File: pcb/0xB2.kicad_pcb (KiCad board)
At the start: 2 copper layers, 17.8 x 33 mm, 37 parts, among them J1 USB_C_Receptacle_USB2.0, J2 Conn_01x12, J3 Conn_01x05, J4 Conn_01x12, SW1 SW_Push, SW2 SW_Push, U1 RP2040, U2 W25Q32JVZP, U3 AP2127K-3.3, Y1 Crystal_GND24

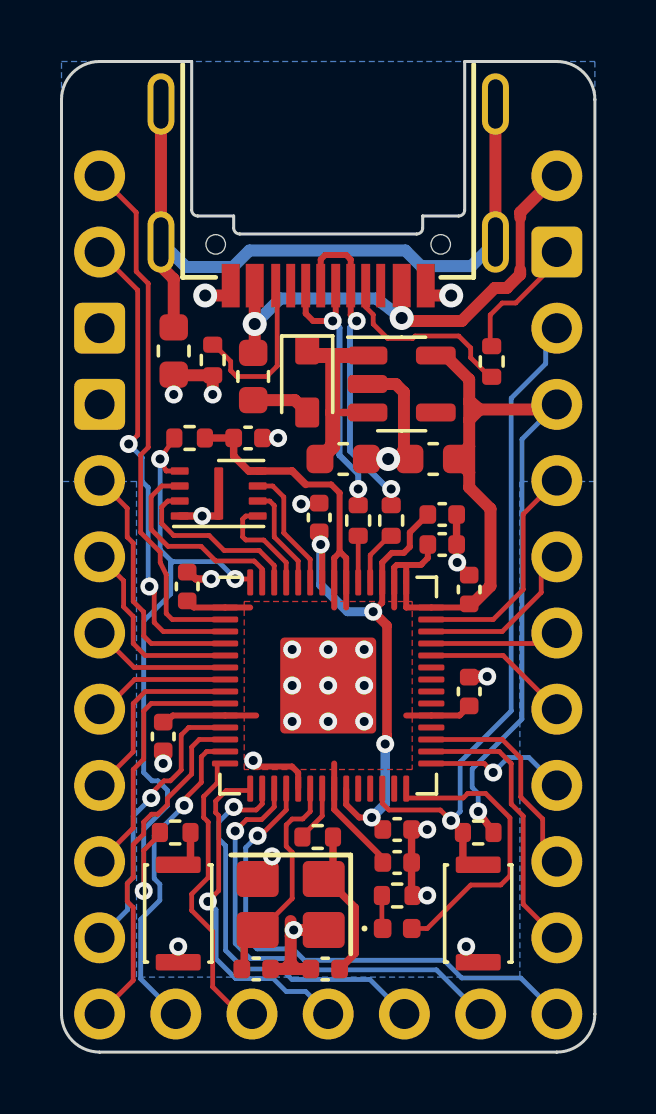
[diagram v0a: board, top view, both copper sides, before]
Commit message: Minor routing corrections
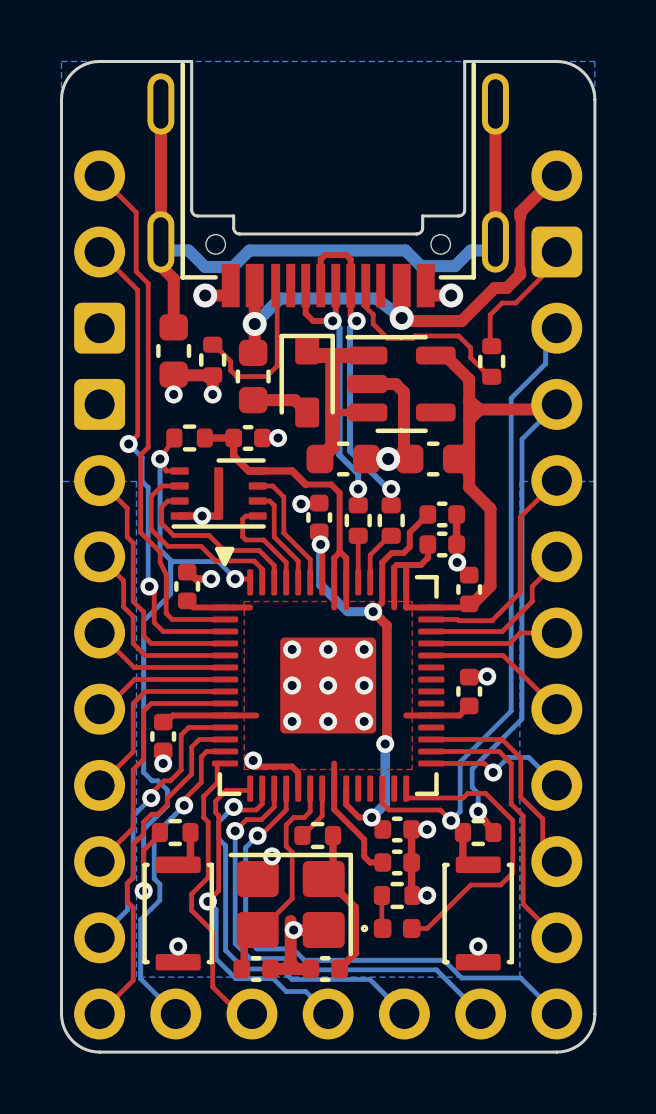
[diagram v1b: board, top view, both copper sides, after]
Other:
- board text added: "0xB2 v1"

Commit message: Add silkscreen drawing
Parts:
- added rb_cake: G*****, 0xB2_drawings:rb_cake, B.Cu at (155.9, 94.7)

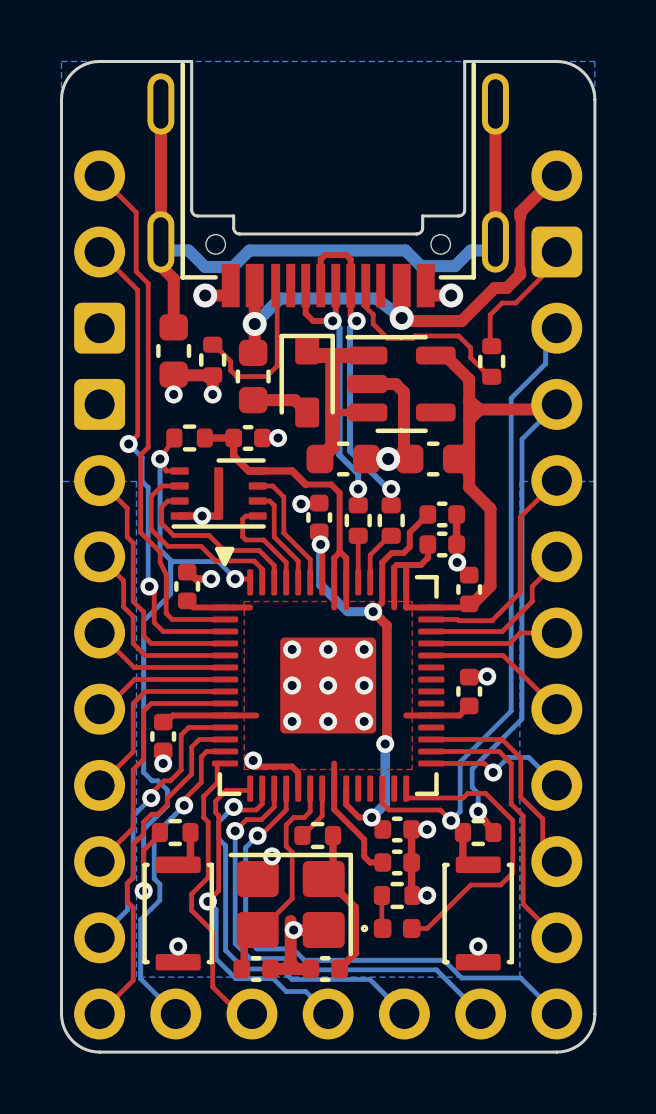
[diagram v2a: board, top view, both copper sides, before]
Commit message: Smaller crystal footprint > 2520
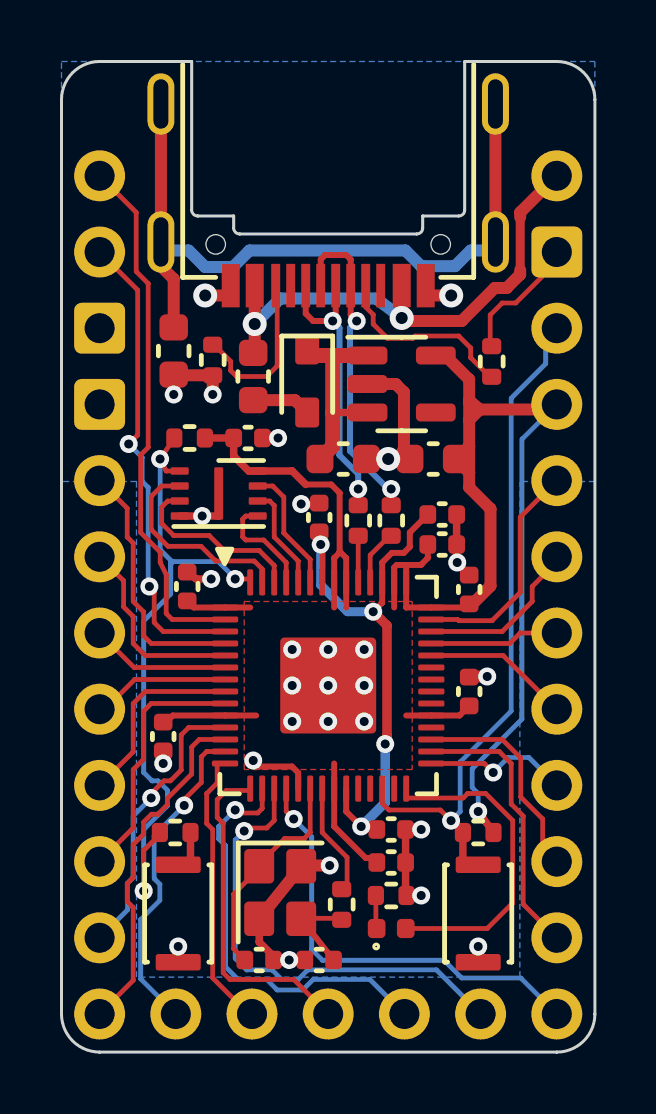
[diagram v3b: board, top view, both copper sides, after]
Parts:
- Y1: footprint Crystal:Crystal_SMD_3225-4Pin_3.2x2.5mm -> Crystal:Crystal_SMD_2520-4Pin_2.5x2.0mm
- moved R8 2.44 mm to (152.8, 104.3), turned to 90 degrees
- moved Y1 0.53 mm to (150.8, 103.9), turned to -90 degrees
- moved C4 0.36 mm to (152.1, 106.2)
- moved C3 0.32 mm to (150.1, 106.2)
- moved C14 0.20 mm to (154.5, 102.9)
- moved C8 0.20 mm to (154.5, 101.8)
- moved D1 0.20 mm to (154.5, 105.1)
- moved R1 0.20 mm to (154.5, 104.0)
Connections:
- Y1 pad 1: Net-(C4-Pad1) -> Net-(C3-Pad1)
- Y1 pad 3: Net-(C3-Pad1) -> Net-(C4-Pad1)
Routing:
- net /D15: track 17.0 -> 14.8 mm
- net Net-(C4-Pad1): track 5.14 -> 3.20 mm
- net Net-(R8-Pad2): track 1.89 -> 3.77 mm
- net GND: track 32.4 -> 34.0 mm
- net Net-(C3-Pad1): track 6.47 -> 7.30 mm
- net /LED: track 10.2 -> 11.0 mm
- net /D11: track 10.2 -> 9.45 mm
- net /D14: track 15.1 -> 15.8 mm
- net /D13: track 13.5 -> 14.1 mm
- net /D12: track 11.4 -> 11.2 mm, vias 1 -> 0

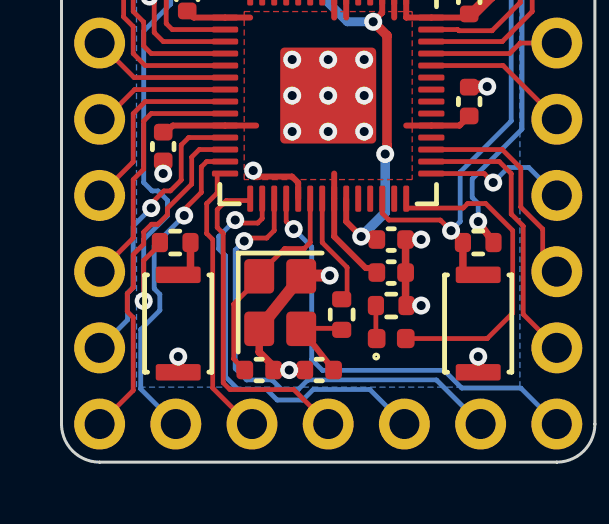
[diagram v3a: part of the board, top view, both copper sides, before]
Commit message: Add BOOT pad on bottom layer
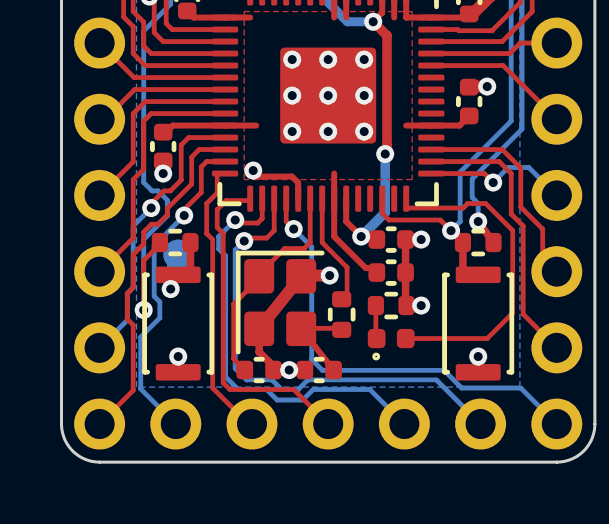
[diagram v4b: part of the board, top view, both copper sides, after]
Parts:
- added J5: Conn_01x01, TestPoint:TestPoint_Pad_D1.0mm, B.Cu at (147.4, 102.3)
- C3, C4: value 27p -> 15p
- U3: value AP2127K-3.3 -> XC6210B332MR-G
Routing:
- net Net-(R3-Pad1): track 1.38 -> 3.18 mm, vias 0 -> 1
- net /QSPI_~{CS}: track 23.3 -> 23.9 mm

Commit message: Silkscreen update
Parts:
- added splinky: G*****, 0xB2_drawings:splinky, B.Cu at (156.7, 101.4)
- D2: value D_Schottky -> B5817
- moved rb_cake 3.15 mm to (155.8, 91.6)
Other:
- board text added: "0xB2"
- board text added: "v1"
- board text removed: "0xB2 v1"

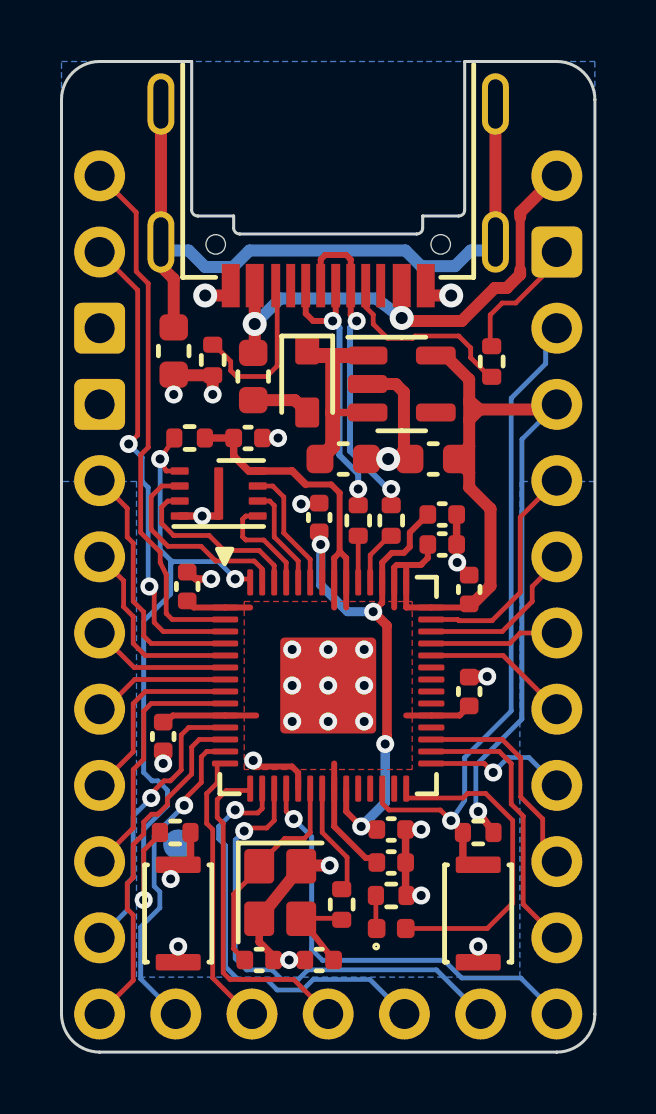
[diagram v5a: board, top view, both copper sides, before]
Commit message: Add USB VBUS detect on GPIO 25
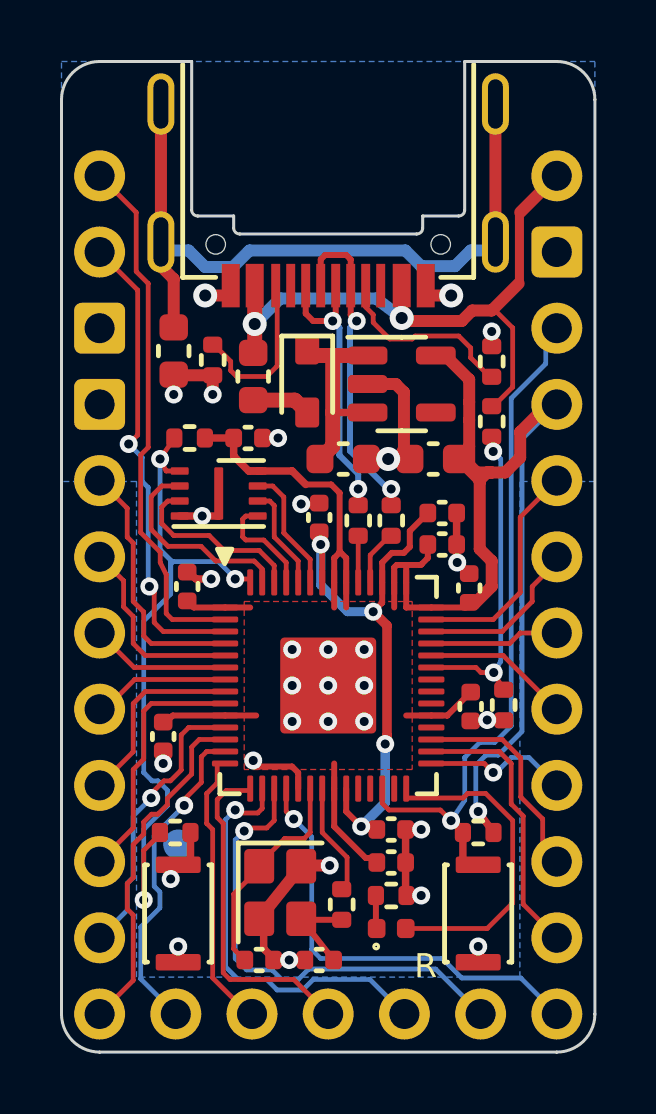
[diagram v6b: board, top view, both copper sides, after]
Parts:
- added R10: 5.1k, Resistor_SMD:R_0402_1005Metric, F.Cu at (157.8, 88.2)
- added R11: 10k, Resistor_SMD:R_0402_1005Metric, F.Cu at (158.2, 97.7)
- moved C13 0.50 mm to (157.2, 97.7), turned to -90 degrees
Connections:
- U1 pad 37: unconnected-(U1-Pad37) -> /VBUS_DET
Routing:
- net /VBUS_DET: track 0.00 -> 10.4 mm, vias 0 -> 2
- net VBUS: track 17.2 -> 21.1 mm
- net GND: track 34.0 -> 30.7 mm, vias 28 -> 29
- net +3V3: track 59.8 -> 61.5 mm
